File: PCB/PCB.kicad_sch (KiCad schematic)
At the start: 0 parts

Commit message: pcb update
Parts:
- added IC1: MSPM0G3507SPTR, SpinnyKitty:MSPM0G3507SPTR, symbol MSPM0G3507SPTR:MSPM0G3507SPTR
- added J1: ICS43434 Breakout, Connector_PinSocket_1.00mm:PinSocket_1x06_P1.00mm_Vertical, symbol SpinnyKitty:ICS43434 Breakout
- added J2: MAX98357_Breakout, SpinnyKitty:MAX98357, symbol SpinnyKitty:MAX98357_Breakout
- added J4: LED_Header, Connector_PinHeader_2.54mm:PinHeader_1x03_P2.54mm_Vertical, symbol SpinnyKitty:LED_Header
- added J5: MSPM0 Programming Header, Connector_PinHeader_2.54mm:PinHeader_1x05_P2.54mm_Vertical, symbol SpinnyKitty:MSPM0 Programming Header
- added J6: USBC_Power_Breakout, SpinnyKitty:USBC_POWER_BREAKOUT, symbol SpinnyKitty:USBC_Power_Breakout
- added M1: Motor_DC, symbol Motor:Motor_DC
- added U1: ~, SpinnyKitty:ESP32_30pin, symbol esp32_30pin_revised:ESP32_30Pin
- added U2: 254, SpinnyKitty:MODULE_254, symbol 254:254

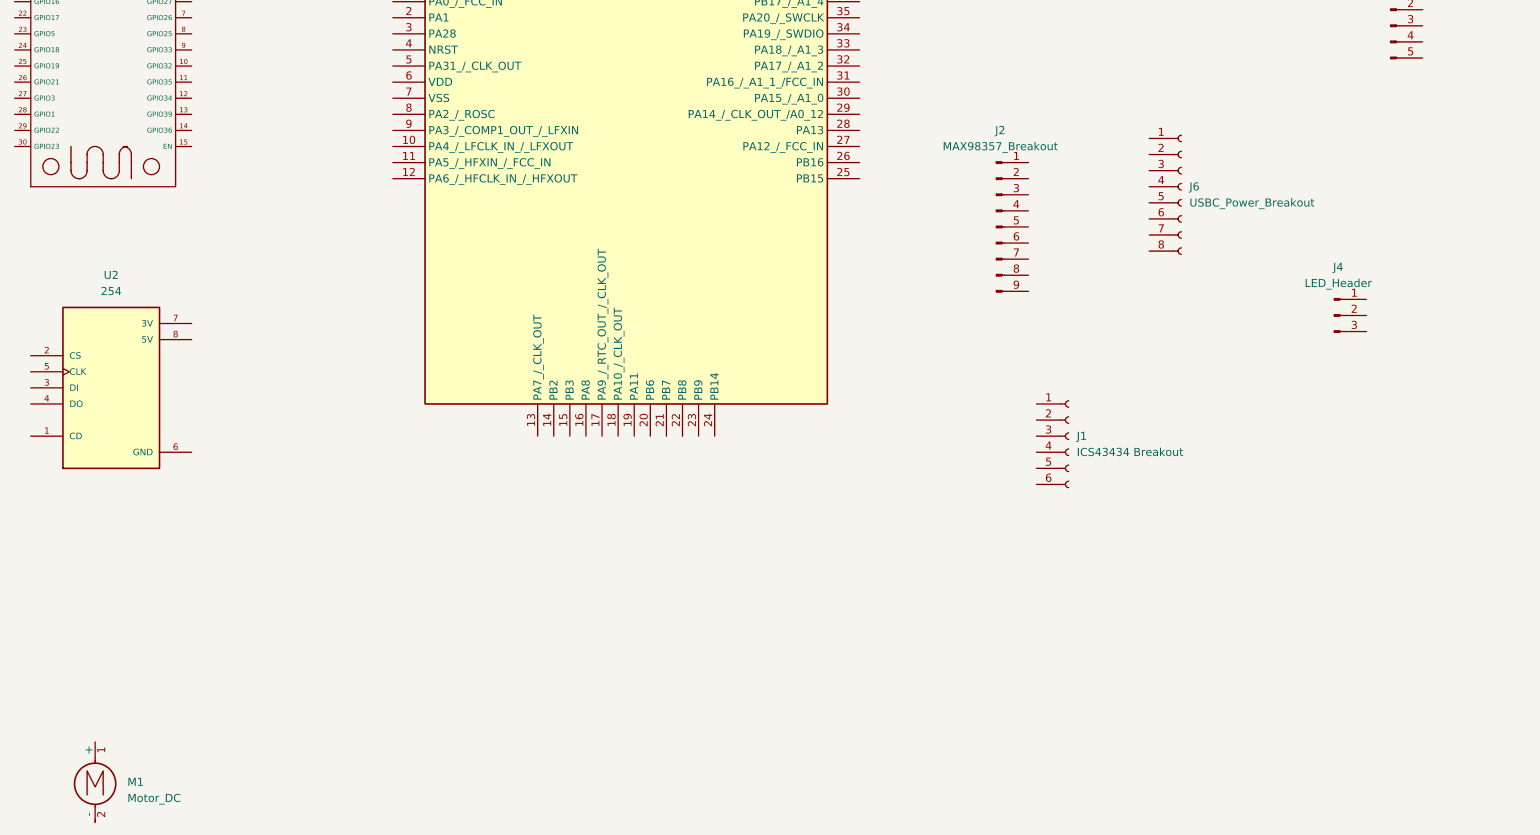
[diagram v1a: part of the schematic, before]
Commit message: all symbols and footprints
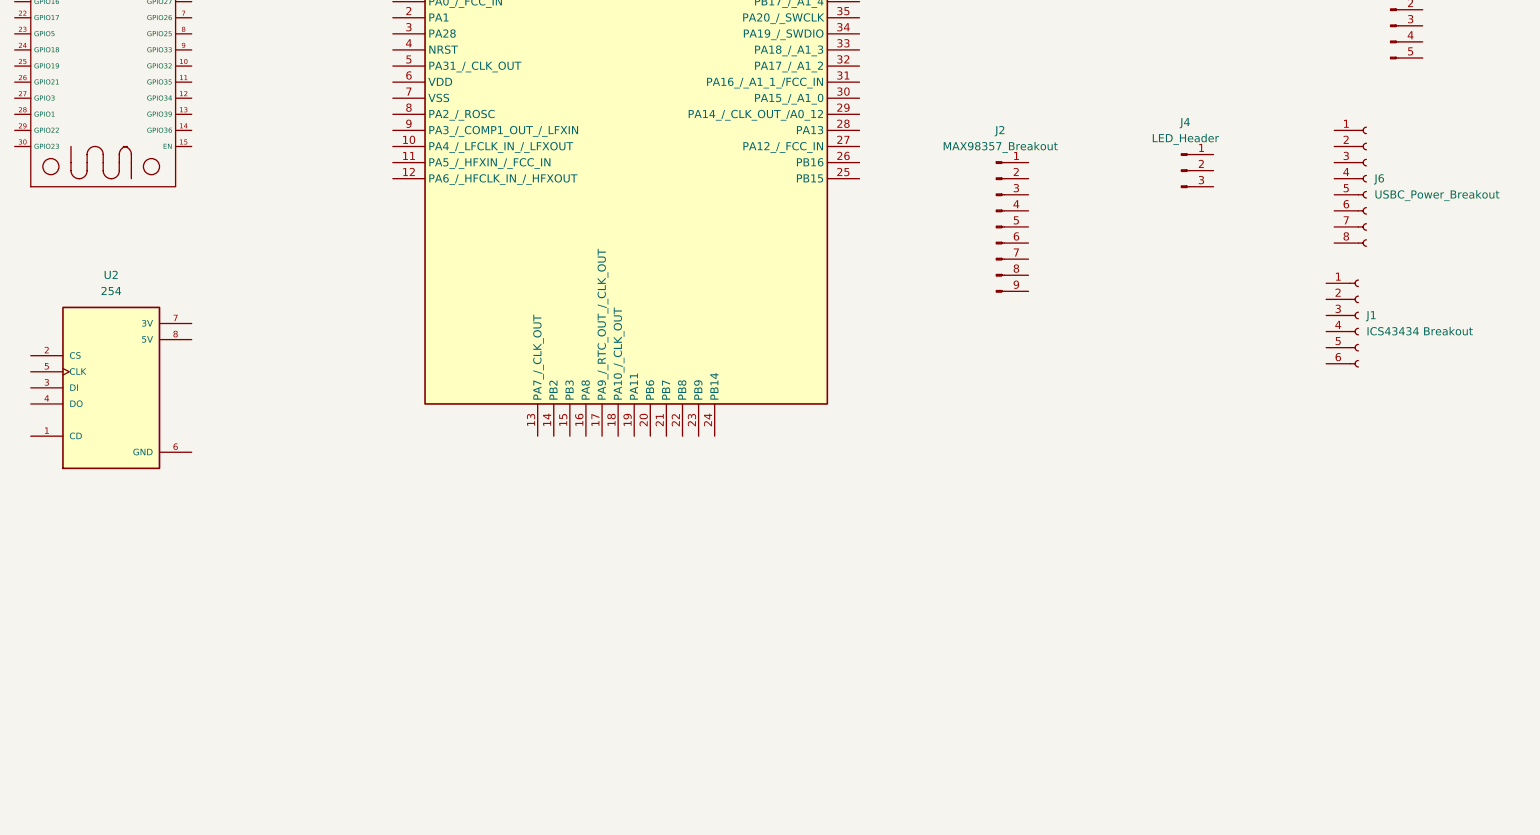
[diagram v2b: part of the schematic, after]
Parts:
- removed M1: Motor_DC, symbol Motor:Motor_DC
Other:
- moved on the sheet: J1, J4, J6
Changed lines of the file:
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@@
 	(symbol
 		(lib_id "SpinnyKitty:ICS43434 Breakout")
-		(at 209.55 129.54 0)
+		(at 255.27 110.49 0)
 		(unit 1)
 		(exclude_from_sim no)
@@
 		(fields_autoplaced yes)
 		(property "Reference" "J1"
-			(at 210.82 129.5399 0)
+			(at 256.54 110.4899 0)
 			(effects
 				(font
@@
 		)
 		(property "Value" "ICS43434 Breakout"
-			(at 210.82 132.0799 0)
+			(at 256.54 113.0299 0)
 			(effects
 				(font
@@
 		)
 		(property "Footprint" "Connector_PinSocket_1.00mm:PinSocket_1x06_P1.00mm_Vertical"
-			(at 209.55 129.54 0)
+			(at 255.27 110.49 0)
 			(effects
 				(font
@@
 		)
 		(property "Datasheet" "~"
-			(at 209.55 129.54 0)
+			(at 255.27 110.49 0)
 			(effects
 				(font
@@
 		)
 		(property "Description" "Generic connector, single row, 01x06, script generated"
-			(at 209.55 129.54 0)
+			(at 255.27 110.49 0)
 			(effects
 				(font
@@
 	(symbol
 		(lib_id "SpinnyKitty:LED_Header")
-		(at 251.46 110.49 0)
+		(at 227.33 87.63 0)
 		(unit 1)
 		(exclude_from_sim no)
@@
 		(fields_autoplaced yes)
 		(property "Reference" "J4"
-			(at 252.095 102.87 0)
+			(at 227.965 80.01 0)
 			(effects
 				(font
@@
 		)
 		(property "Value" "LED_Header"
-			(at 252.095 105.41 0)
+			(at 227.965 82.55 0)
 			(effects
 				(font
@@
 		)
 		(property "Footprint" "Connector_PinHeader_2.54mm:PinHeader_1x03_P2.54mm_Vertical"
-			(at 251.46 110.49 0)
+			(at 227.33 87.63 0)
 			(effects
 				(font
@@
 		)
 		(property "Datasheet" "~"
-			(at 251.46 110.49 0)
+			(at 227.33 87.63 0)
 			(effects
 				(font
@@
 		)
 		(property "Description" "Generic connector, single row, 01x03, script generated"
-			(at 251.46 110.49 0)
+			(at 227.33 87.63 0)
 			(effects
 				(font
@@
 	)
 	(symbol
-		(lib_id "Motor:Motor_DC")
-		(at 55.88 182.88 0)
-		(unit 1)
-		(exclude_from_sim no)
-		(in_bom yes)
-		(on_board yes)
-		(dnp no)
-		(fields_autoplaced yes)
-		(property "Reference" "M1"
-			(at 60.96 184.1499 0)
-			(effects
-				(font
-					(size 1.27 1.27)
-				)
-				(justify left)
-			)
-		)
-		(property "Value" "Motor_DC"
-			(at 60.96 186.6899 0)
-			(effects
-				(font
-					(size 1.27 1.27)
-				)
-				(justify left)
-			)
-		)
-		(property "Footprint" ""
-			(at 55.88 185.166 0)
-			(effects
-				(font
-					(size 1.27 1.27)
-				)
-				(hide yes)
-			)
-		)
-		(property "Datasheet" "~"
-			(at 55.88 185.166 0)
-			(effects
-				(font
-					(size 1.27 1.27)
-				)
-				(hide yes)
-			)
-		)
-		(property "Description" "DC Motor"
-			(at 55.88 182.88 0)
-			(effects
-				(font
-					(size 1.27 1.27)
-				)
-				(hide yes)
-			)
-		)
-		(pin "1"
-		)
-		(pin "2"
-		)
-		(instances
-			(project ""
-				(path "/954dff68-cc85-452c-9053-ce35508878d2"
-					(reference "M1")
-					(unit 1)
-				)
-			)
-		)
-	)
-	(symbol
 		(lib_id "SpinnyKitty:MSPM0 Programming Header")
 		(at 260.35 64.77 0)
@@
 	(symbol
 		(lib_id "SpinnyKitty:USBC_Power_Breakout")
-		(at 227.33 90.17 0)
+		(at 256.54 88.9 0)
 		(unit 1)
 		(exclude_from_sim no)
@@
 		(fields_autoplaced yes)
 		(property "Reference" "J6"
-			(at 228.6 90.1699 0)
+			(at 257.81 88.8999 0)
 			(effects
 				(font
@@
 		)
 		(property "Value" "USBC_Power_Breakout"
-			(at 228.6 92.7099 0)
+			(at 257.81 91.4399 0)
 			(effects
 				(font
@@
 		)
 		(property "Footprint" "SpinnyKitty:USBC_POWER_BREAKOUT"
-			(at 227.33 90.17 0)
+			(at 256.54 88.9 0)
 			(effects
 				(font
@@
 		)
 		(property "Datasheet" "~"
-			(at 227.33 90.17 0)
+			(at 256.54 88.9 0)
 			(effects
 				(font
@@
 		)
 		(property "Description" "Generic connector, single row, 01x08, script generated"
-			(at 227.33 90.17 0)
-			(effects
-				(font
+			(at 256.54 88.9 0)
+			(effects
+				(font

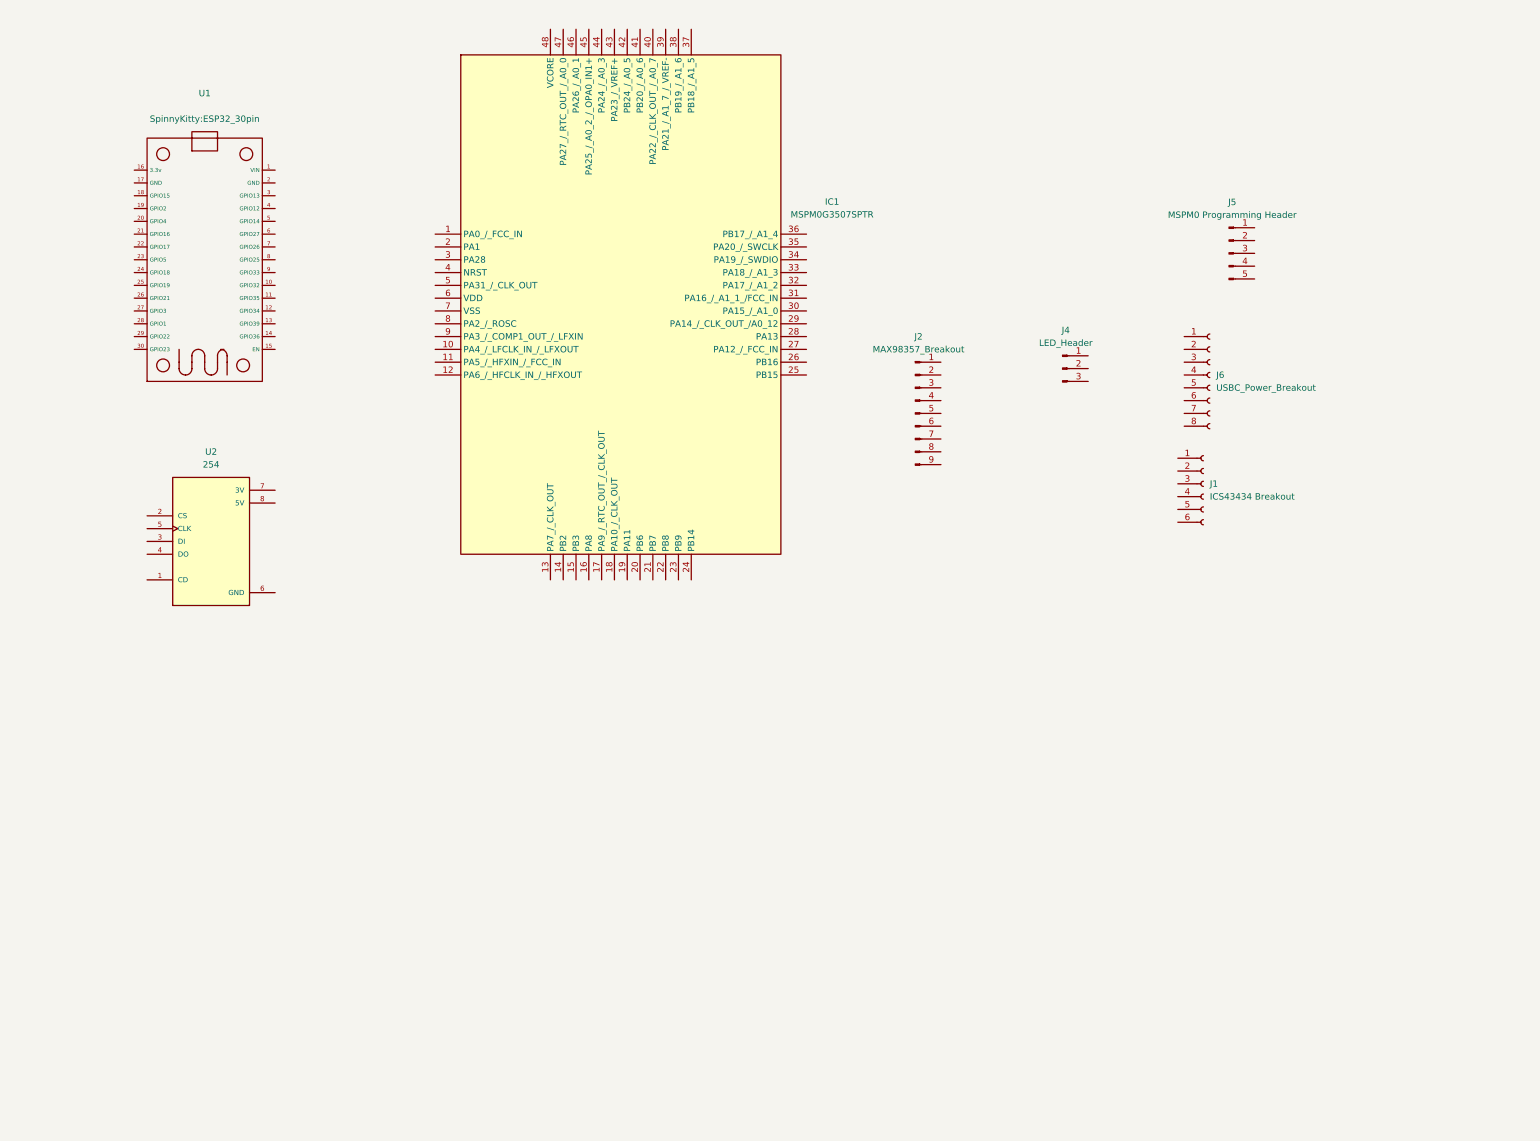
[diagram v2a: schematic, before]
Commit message: schematic for on board power system
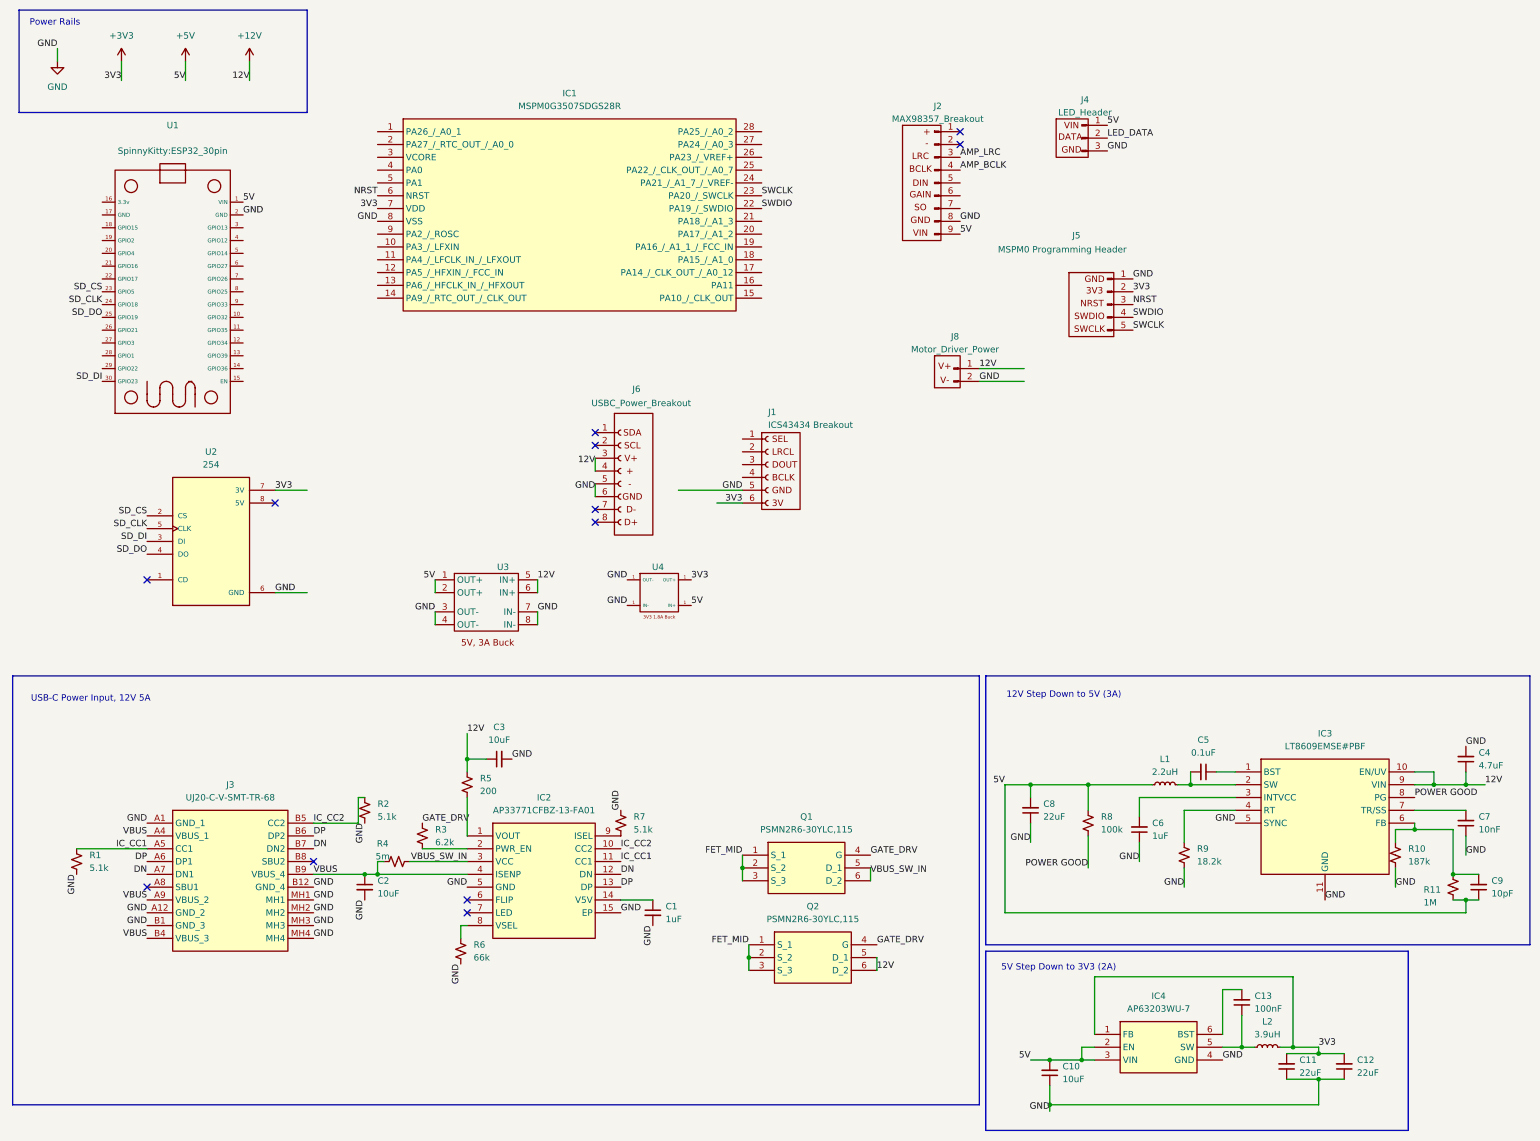
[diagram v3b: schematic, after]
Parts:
- removed IC1: MSPM0G3507SPTR, SpinnyKitty:MSPM0G3507SPTR, symbol MSPM0G3507SPTR:MSPM0G3507SPTR
- added C1, C6: 1uF, Capacitor_SMD:C_0805_2012Metric_Pad1.18x1.45mm_HandSolder, symbol Device:C_Small
- added C10, C2, C3: 10uF, Capacitor_SMD:C_1206_3216Metric_Pad1.33x1.80mm_HandSolder, symbol Device:C_Small
- added C11, C12, C8: 22uF, Capacitor_SMD:C_1206_3216Metric_Pad1.33x1.80mm_HandSolder, symbol Device:C_Small
- added C13: 100nF, Capacitor_SMD:C_0805_2012Metric_Pad1.18x1.45mm_HandSolder, symbol Device:C_Small
- added C4: 4.7uF, Capacitor_SMD:C_0805_2012Metric_Pad1.18x1.45mm_HandSolder, symbol Device:C_Small
- added C5: 0.1uF, Capacitor_SMD:C_0805_2012Metric_Pad1.18x1.45mm_HandSolder, symbol Device:C_Small
- added C7: 10nF, Capacitor_SMD:C_0805_2012Metric_Pad1.18x1.45mm_HandSolder, symbol Device:C_Small
- added C9: 10pF, Capacitor_SMD:C_0805_2012Metric_Pad1.18x1.45mm_HandSolder, symbol Device:C_Small
- added IC1: MSPM0G3507SDGS28R, SOP50P490X110-28N, symbol MSPM0G3507SDGS28R:MSPM0G3507SDGS28R
- added IC2: AP33771CFBZ-13-FA01, SpinnyKitty:AP33771CFBZ13FA01, symbol AP33771CFBZ-13-FA01:AP33771CFBZ-13-FA01
- added IC3: LT8609EMSE#PBF, SpinnyKitty:SOP50P490X110-11N, symbol LT8609EMSE#PBF:LT8609EMSE#PBF
- added IC4: AP63203WU-7, SpinnyKitty:AP63203WU7, symbol AP63203WU-7:AP63203WU-7
- added J3: UJ20-C-V-SMT-TR-68, SpinnyKitty:UJ20CVSMTTR68, symbol UJ20-C-V-SMT-TR-68:UJ20-C-V-SMT-TR-68
- added J8: Motor_Driver_Power, Connector_PinHeader_2.54mm:PinHeader_1x02_P2.54mm_Vertical, symbol SpinnyKitty:Motor_Driver_Power
- added L1: 2.2uH, SpinnyKitty:PM5402222NLT, symbol Device:L_Small
- added L2: 3.9uH, SpinnyKitty:SRR3818A3R9Y, symbol Device:L_Small
- added Q1, Q2: PSMN2R6-30YLC,115, SpinnyKitty:PSMN2R630YLC115, symbol PSMN2R6-30YLC_115:PSMN2R6-30YLC,115
- added R1, R2, R7: 5.1k, Resistor_SMD:R_0603_1608Metric_Pad0.98x0.95mm_HandSolder, symbol Device:R_Small_US
- added R10: 187k, Resistor_SMD:R_0603_1608Metric_Pad0.98x0.95mm_HandSolder, symbol Device:R_Small_US
- added R11: 1M, Resistor_SMD:R_0603_1608Metric_Pad0.98x0.95mm_HandSolder, symbol Device:R_Small_US
- added R3: 6.2k, Resistor_SMD:R_0603_1608Metric_Pad0.98x0.95mm_HandSolder, symbol Device:R_Small_US
- added R4: 5m, Resistor_SMD:R_2512_6332Metric_Pad1.40x3.35mm_HandSolder, symbol Device:R_Small_US
- added R5: 200, Resistor_SMD:R_0603_1608Metric_Pad0.98x0.95mm_HandSolder, symbol Device:R_Small_US
- added R6: 66k, Resistor_SMD:R_0603_1608Metric_Pad0.98x0.95mm_HandSolder, symbol Device:R_Small_US
- added R8: 100k, Resistor_SMD:R_0603_1608Metric_Pad0.98x0.95mm_HandSolder, symbol Device:R_Small_US
- added R9: 18.2k, Resistor_SMD:R_0603_1608Metric_Pad0.98x0.95mm_HandSolder, symbol Device:R_Small_US
- added U3: ~, SpinnyKitty:5V 3A Buck, symbol SpinnyKitty:5V3A_Buck
- added U4: ~, symbol SpinnyKitty:3V3_1.8A_Buck
- J1: footprint Connector_PinSocket_1.00mm:PinSocket_1x06_P1.00mm_Vertical -> SpinnyKitty:ICS43434 Breakout; now left out of the parts list
- J2, J4, J5, J6, U1, U2: now left out of the parts list
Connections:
- net AMP_LRC: now reaches J2.3 (LRC)
- net AMP_BCLK: now reaches J2.4 (BCLK)
- net GND: now reaches J2.8 (GND)
- net GND: now also J1.5 (GND), J4.3 (GND), J5.1 (GND), J6.5 (-), J6.6 (GND), U1.2 (GND), U2.6 (GND), C1.2, C10.1, C11.1, C12.1, C2.2, C3.2, C4.2, C6.1, C7.1, C8.1, IC1.8 (VSS), IC2.15 (EP), IC2.5 (GND), IC3.11 (GND), IC3.5 (SYNC), IC4.4 (GND), J3.A1 (GND_1), J3.A12 (GND_2), J3.B1 (GND_3), J3.B12 (GND_4), J3.MH1, J3.MH2, J3.MH3, J3.MH4, J8.2 (V-), R1.2, R10.2, R2.2, R6.2, R7.1, R9.2, U3.3 (OUT-), U3.4 (OUT-), U3.7 (IN-), U3.8 (IN-), U4.1 (IN+)
- net +5V: now reaches J2.9 (VIN)
- net +5V: now also J4.1 (VIN), U1.1 (VIN), C10.2, C8.2, C9.1, IC4.2 (EN), IC4.3 (VIN), L1.1, R11.2, R8.1, U3.1 (OUT+), U3.2 (OUT+), U4.1 (IN+)
- net +3V3: now reaches J1.6 (3V)
- net +3V3: now also J5.2 (3V3), U2.7 (3V), C11.2, C12.2, IC1.7 (VDD), IC4.1 (FB), L2.2, U4.1 (IN+)
- net LED_DATA: now reaches J4.2 (DATA)
- net SD_CS: now reaches U2.2 (CS)
- net SD_CS: now also U1.23 (GPIO5)
- net SD_DI: now reaches U2.3 (DI)
- net SD_DI: now also U1.30 (GPIO23)
- net SD_DO: now reaches U2.4 (DO)
- net SD_DO: now also U1.25 (GPIO19)
- net SD_CLK: now reaches U2.5 (CLK)
- net SD_CLK: now also U1.24 (GPIO18)
- net NRST: now reaches J5.3 (NRST)
- net NRST: now also IC1.6 (NRST)
- net SWDIO: now reaches J5.4 (SWDIO)
- net SWDIO: now also IC1.22 (PA19_/_SWDIO)
- net SWCLK: now reaches J5.5 (SWCLK)
- net SWCLK: now also IC1.23 (PA20_/_SWCLK)
- net +12V: now reaches J6.3 (V+)
- net +12V: now also J6.4 (+), C3.1, C4.1, IC3.10 (EN/UV), IC3.9 (VIN), J8.1 (V+), Q2.5 (D_1), Q2.6 (D_2), R5.1, U3.5 (IN+), U3.6 (IN+)
- new net: C5.2, IC3.2 (SW), L1.2
- new net: C13.1, IC4.5 (SW), L2.1
- new net: IC2.8 (VSEL), R6.1
- new net: IC2.2 (PWR_EN), R3.2
- new net: IC2.1 (VOUT), R5.2
- new net: C6.2, IC3.3 (INTVCC)
- new net: C5.1, IC3.1 (BST)
- new net: IC3.4 (RT), R9.1
- new net: C1.1, IC2.14 (V5V)
- new net: IC2.9 (ISEL), R7.2
- new net: C9.2, IC3.6 (FB), R10.1, R11.1
- new net: C13.2, IC4.6 (BST)
- new net: C7.2, IC3.7 (TR/SS)
- new net DN: IC2.12 (DN), J3.A7 (DN1), J3.B7 (DN2)
- new net DP: IC2.13 (DP), J3.A6 (DP1), J3.B6 (DP2)
- new net FET_MID: Q1.1 (S_1), Q1.2 (S_2), Q1.3 (S_3), Q2.1 (S_1), Q2.2 (S_2), Q2.3 (S_3)
- new net GATE_DRV: Q1.4 (G), Q2.4 (G), R3.1
- new net IC_CC1: IC2.11 (CC1), J3.A5 (CC1), R1.1
- new net IC_CC2: IC2.10 (CC2), J3.B5 (CC2), R2.1
- new net POWER GOOD: IC3.8 (PG), R8.2
- new net VBUS: C2.1, IC2.4 (ISENP), J3.A4 (VBUS_1), J3.A9 (VBUS_2), J3.B4 (VBUS_3), J3.B9 (VBUS_4), R4.1
- new net VBUS_SW_IN: IC2.3 (VCC), Q1.5 (D_1), Q1.6 (D_2), R4.2
- no-connect marks 0 -> 12
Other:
- note added: "12V Step Down to 5V (3A)"
- note added: "5V Step Down to 3V3 (2A)"
- note added: "Power Rails"
- note added: "USB-C Power Input, 12V 5A"
- moved on the sheet: U1
